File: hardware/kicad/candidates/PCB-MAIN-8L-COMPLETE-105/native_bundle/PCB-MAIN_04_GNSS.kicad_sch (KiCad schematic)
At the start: 20 parts, among them J9 U.FL-R-SMT-1(60), Q4 Complementary N and P channel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, U5 Single rail-to-rail low-power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, U9 MAX-M10S-00B

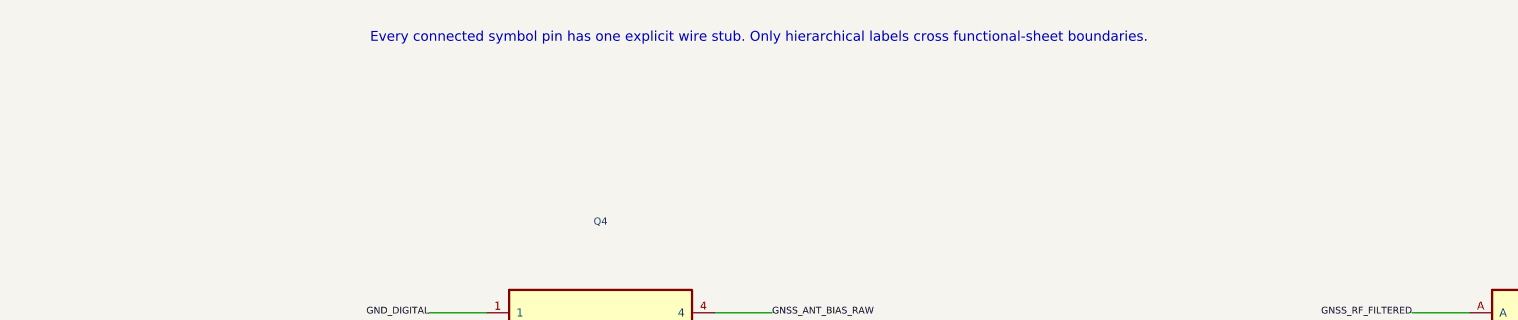
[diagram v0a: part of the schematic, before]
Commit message: PCB-MAIN Rev B: bilingual schematic notes and PDF
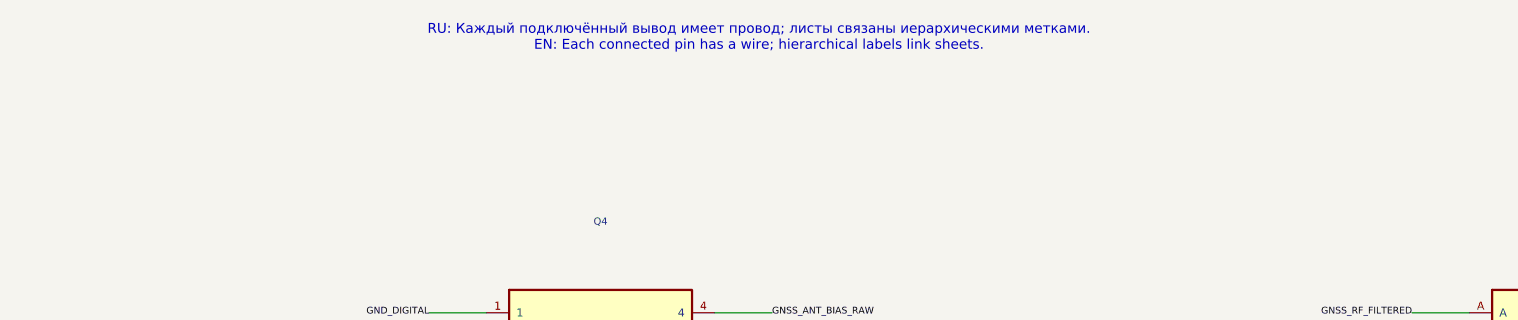
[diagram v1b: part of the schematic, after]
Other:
- note added: "RU: Каждый подключённый вывод имеет провод; листы связаны иерархическими метками. EN: Each connected pin has a wire; hierarchical labels link sheets."
- note removed: "Every connected symbol pin has one explicit wire stub. Only hierarchical labels cross functional-sheet boundaries."
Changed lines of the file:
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@@
     (stroke (width 0.0))
   )
-  (text "Every connected symbol pin has one explicit wire stub. Only hierarchical labels cross functional-sheet boundaries."
+  (text "RU: Каждый подключённый вывод имеет провод; листы связаны иерархическими метками.\nEN: Each connected pin has a wire; hierarchical labels link sheets."
     (at 297.0 12.7 0)
     (effects (font (size 1.1 1.1)))
